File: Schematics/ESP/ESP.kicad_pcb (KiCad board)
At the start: 2 copper layers, 180.5 x 120.6 mm, 77 parts, among them J1 Barrel_Jack, J11 Bumper 1, J12 Bumper 2, J13 Battery Input, J14 Conn_02x19_Odd_Even, J15 UltraSconic B, J16 Conn_02x19_Odd_Even, J2 IMU, J3 Battery charger, J4 Motor A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

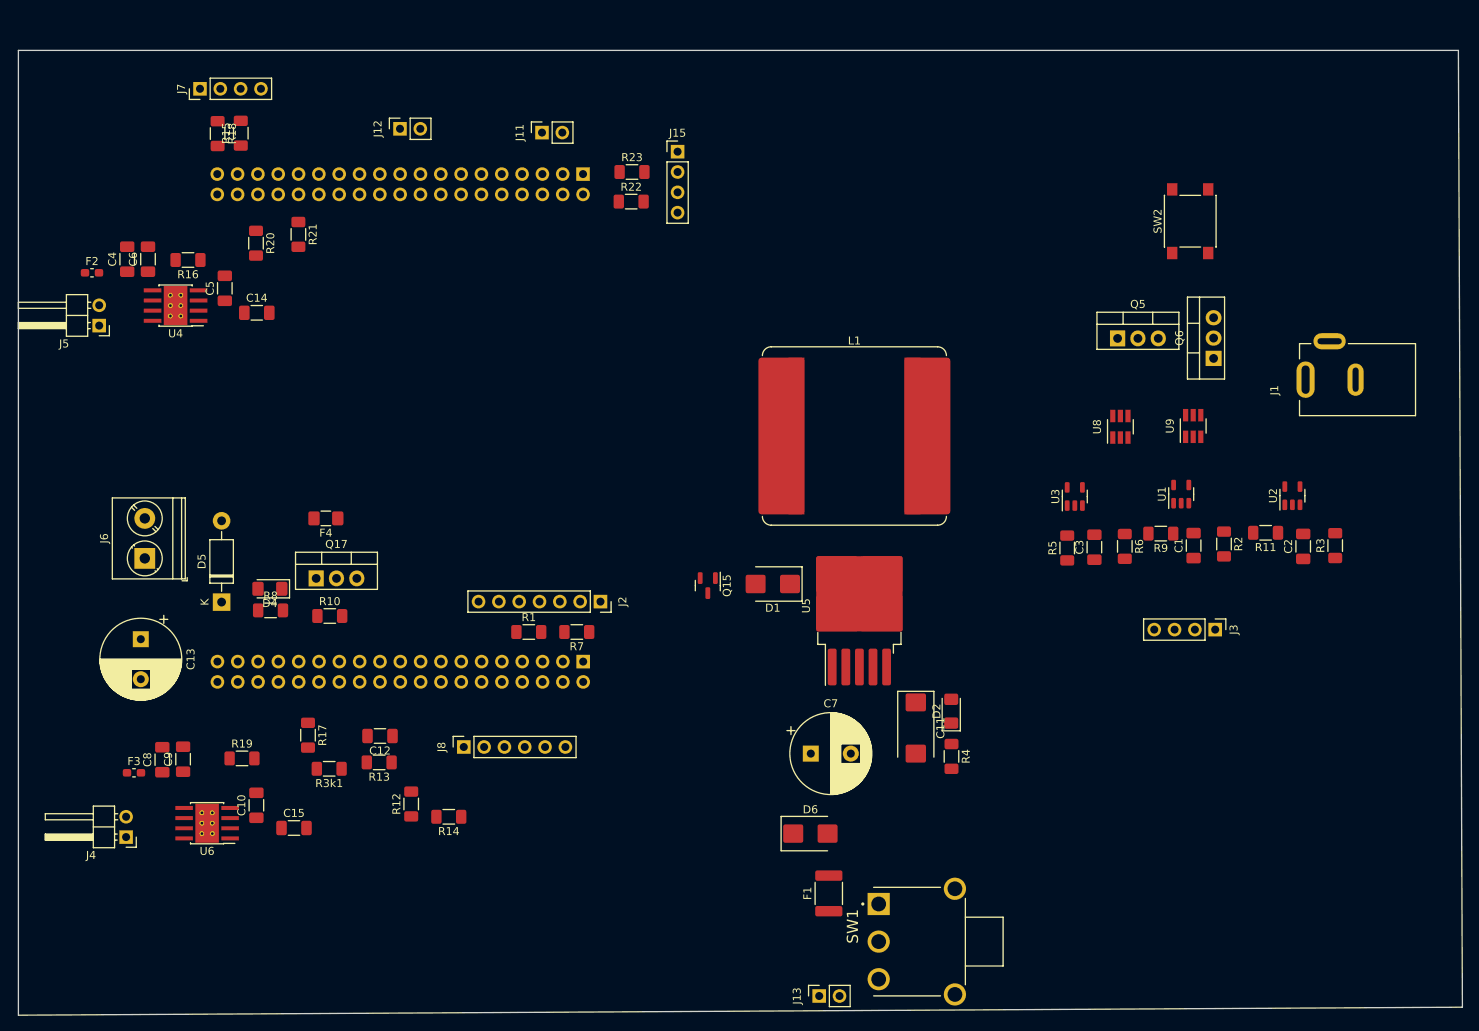
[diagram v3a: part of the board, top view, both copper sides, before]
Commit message: PCB layout done w/wiring only charging part remaining
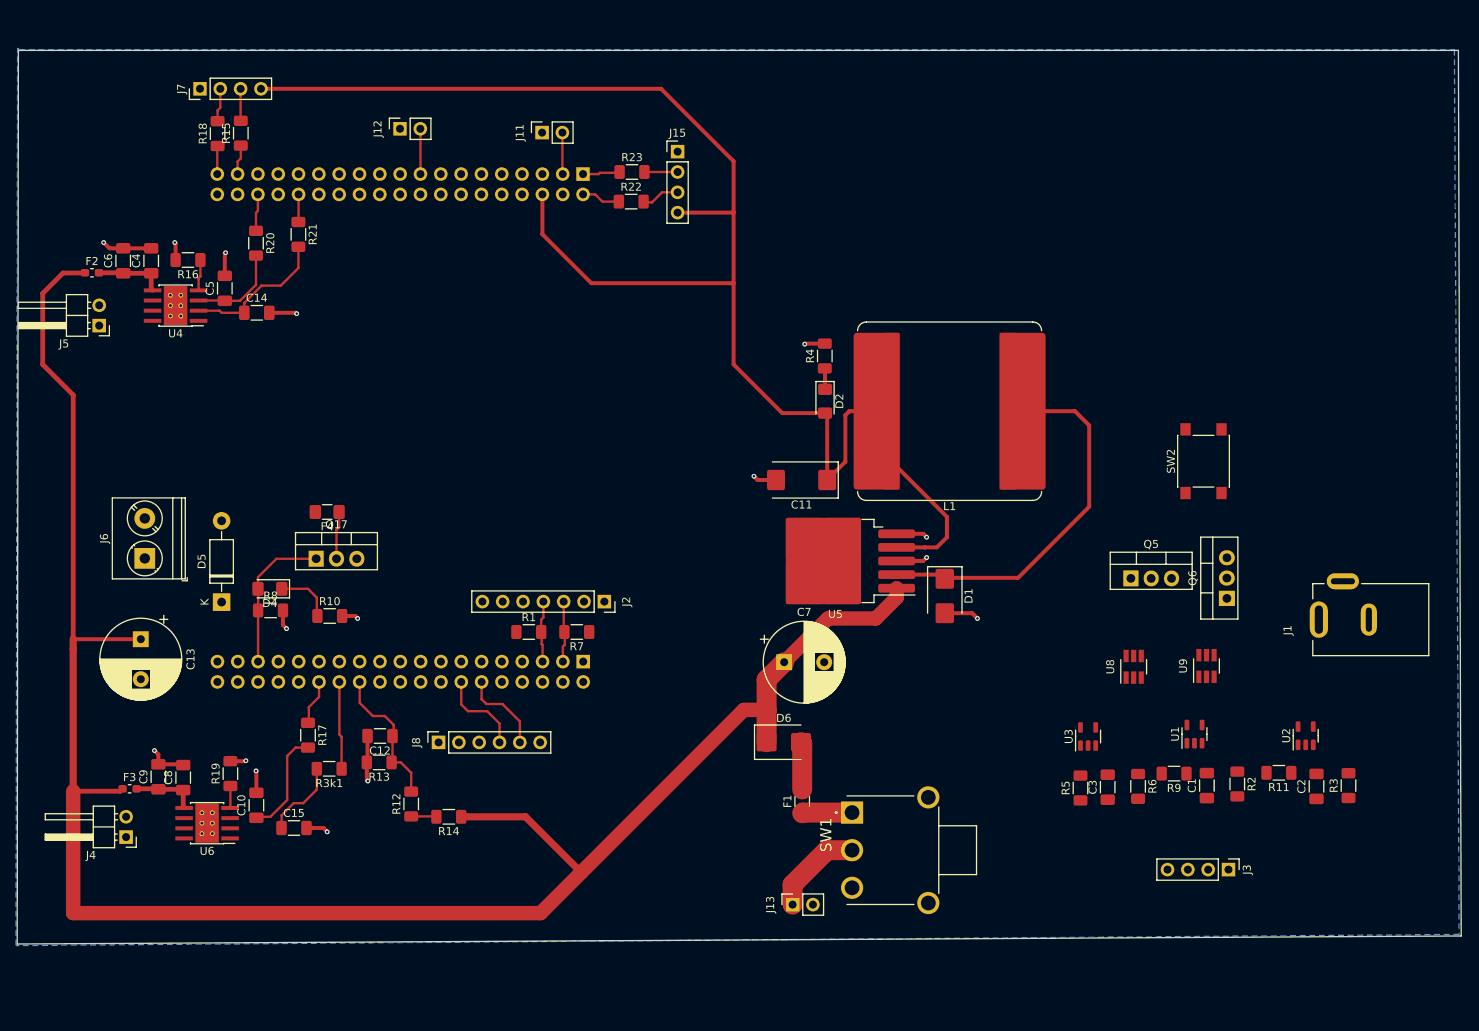
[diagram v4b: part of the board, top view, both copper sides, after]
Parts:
- removed Q15: AO3401A, Package_TO_SOT_SMD:SOT-23
- F1: value 3A -> 5A; footprint Fuse:Fuse_1812_4532Metric_Pad1.30x3.40mm_HandSolder -> Fuse:Fuse_1206_3216Metric_Pad1.42x1.75mm_HandSolder
- F4: value 0.72A -> 0.57A
- moved R4 52.5 mm to (151.1, 98.0), turned to 90 degrees
- moved D2 41.8 mm to (151.1, 103.7), turned to -90 degrees
- moved C11 34.1 mm to (148.2, 113.5), turned to 180 degrees
- moved J1 30.0 mm to (219.1, 131.0)
- moved Q6 30.0 mm to (201.4, 128.3)
- moved C2 30.0 mm to (212.6, 151.8)
- moved R6 30.0 mm to (190.3, 151.8)
- moved Q5 30.0 mm to (189.4, 125.8)
- moved R11 30.0 mm to (207.9, 150.1)
- moved C3 30.0 mm to (186.5, 151.9)
- moved J3 30.0 mm to (201.6, 162.2)
- moved R2 30.0 mm to (202.7, 151.5)
- moved R5 30.0 mm to (183.1, 152.0)
- moved SW2 30.0 mm to (198.4, 111.2)
- moved U2 30.0 mm to (211.2, 145.5)
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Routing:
- net +12V: track 0.00 -> 244.7 mm
- net +5V: track 0.00 -> 188.5 mm
- net Battery-: track 0.00 -> 55.4 mm, vias 0 -> 16
- net Net-(D1-K): track 0.00 -> 47.2 mm
- net Fan Signal: track 0.00 -> 18.8 mm
- net Net-(U4-IN2): track 0.00 -> 18.3 mm
- net Battery level: track 0.00 -> 18.1 mm
- net Net-(U6-IN1): track 0.00 -> 13.3 mm
- net Battery+: track 0.00 -> 11.7 mm
- net Net-(U4-IN1): track 0.00 -> 11.7 mm
- net InputA2: track 0.00 -> 11.0 mm
- net Net-(J16-Pin_14): track 0.00 -> 10.9 mm
- net Net-(J16-Pin_12): track 0.00 -> 10.7 mm
- net Net-(U6-IN2): track 0.00 -> 9.93 mm
- net Net-(U4-VM): track 0.00 -> 8.76 mm
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- added copper zone on B.Cu, net Battery-
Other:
- board size 180.5 x 120.6 mm -> 180.5 x 111.7 mm
- board text removed: "IR 1"
- board text removed: "Voltage Regulator"

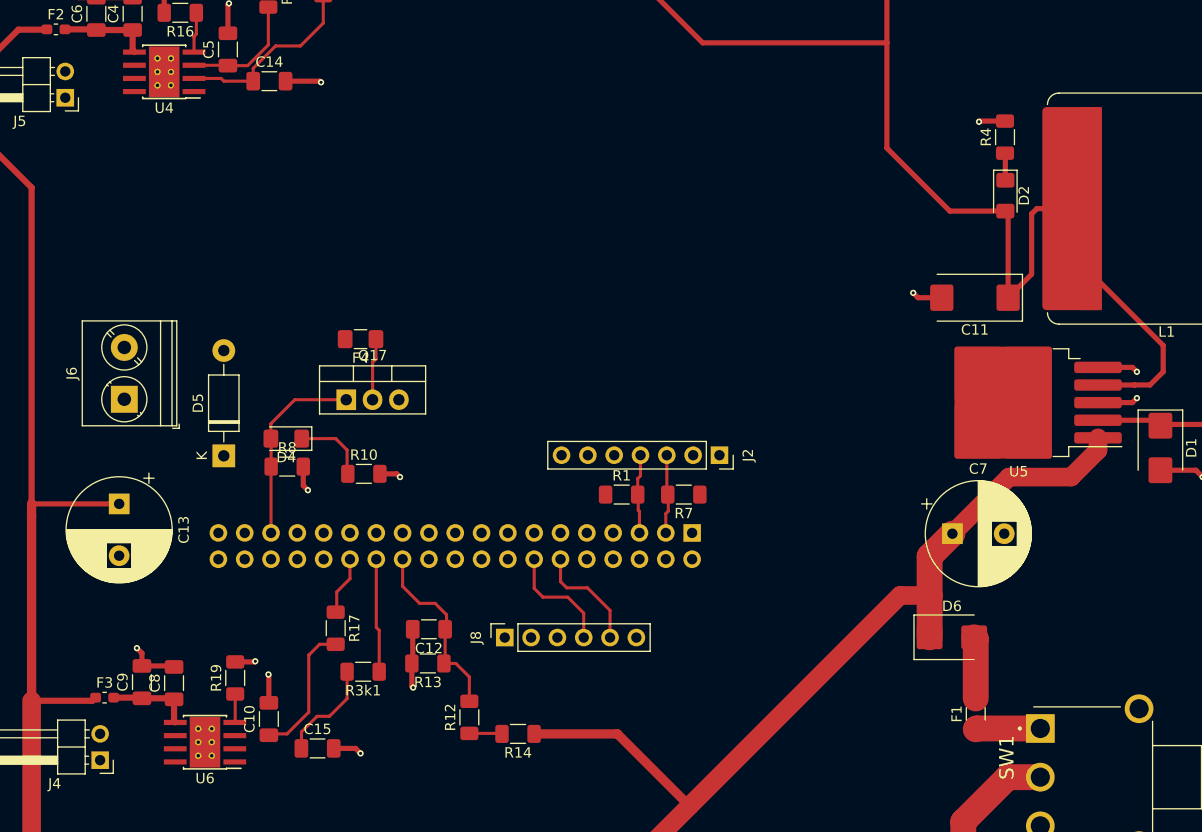
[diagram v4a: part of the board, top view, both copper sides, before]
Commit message: PCB layout done w/wiring only charging part remaining
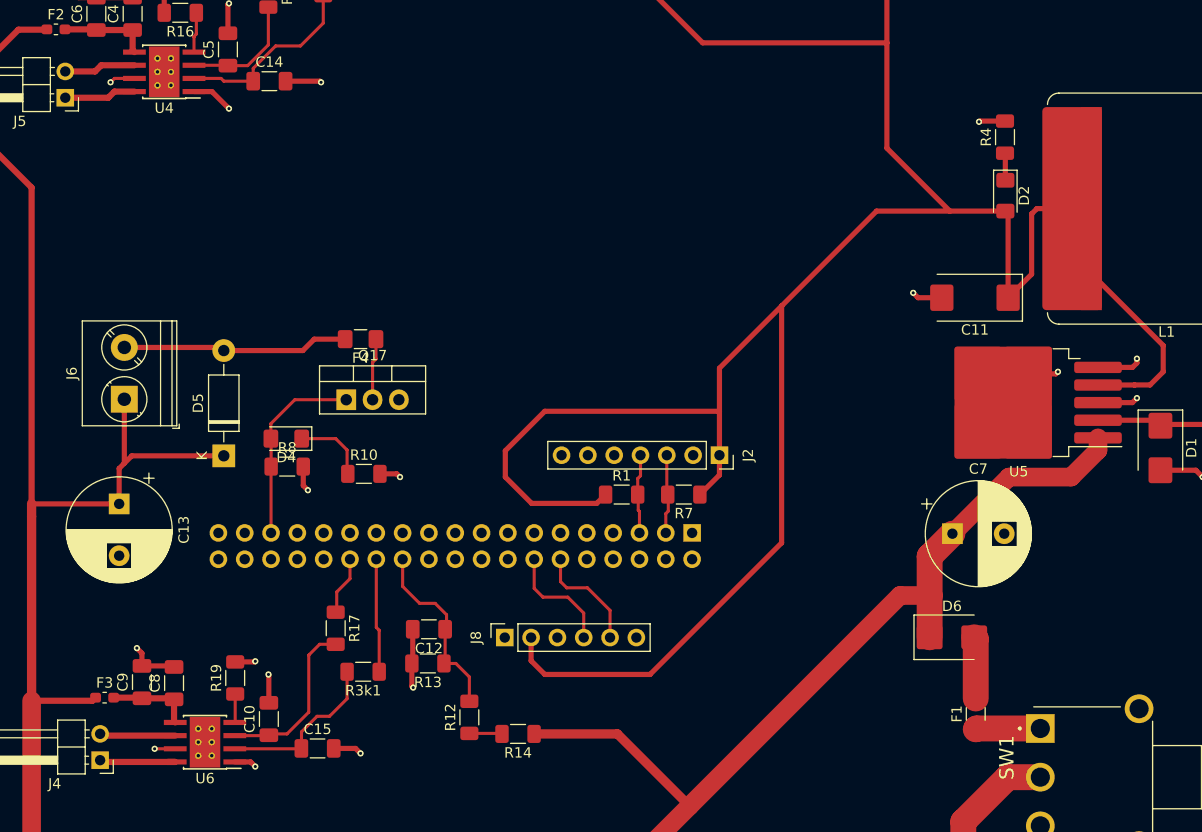
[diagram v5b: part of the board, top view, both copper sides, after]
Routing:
- net +5V: track 188.5 -> 320.9 mm
- net Net-(D5-A): track 0.00 -> 21.9 mm
- net +12V: track 244.7 -> 264.9 mm
- net Battery-: track 55.4 -> 69.4 mm, vias 16 -> 21
- net MotorA-: track 0.00 -> 8.04 mm
- net MotorA+: track 0.00 -> 7.32 mm
- net MotorB-: track 0.00 -> 6.92 mm
- net MotorB+: track 0.00 -> 6.92 mm
- net Net-(U6-IN2): track 9.93 -> 16.4 mm
- net Net-(U6-IN1): track 13.3 -> 16.6 mm
